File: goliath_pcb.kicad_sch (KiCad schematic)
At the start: 95 parts, among them IC1 MCT9001, IC2 MCT9001SD, IC3 MCT9001SD, IC4 MCT9001SD, IC5 MCT9001SD, IC6 MCT9001SD, IC7 MCT9001SD, J1 RJ45_LED, J10 Conn_01x04_Male, J11 Screw_Terminal_01x02, J12 Screw_Terminal_01x02, J13 Screw_Terminal_01x02, J14 Conn_01x02_Male, J15 Conn_01x02_Male, J2 RJ45_LED, J3 RJ45_LED, J4 RJ45_LED, J5 Conn_01x08_Male, J6 Conn_01x08_Male, J7 Conn_01x02_Male, J8 Conn_01x04_Male, J9 Conn_01x04_Male, Q1 STP2N80K5, Q2 STP2N80K5, U1 Pico, U2 LM2592HVT-5.0/NOPB, U3 74HCT244, U4 74HCT244, U5 MCP3008, U6 PCF8574, U7 PCF8574

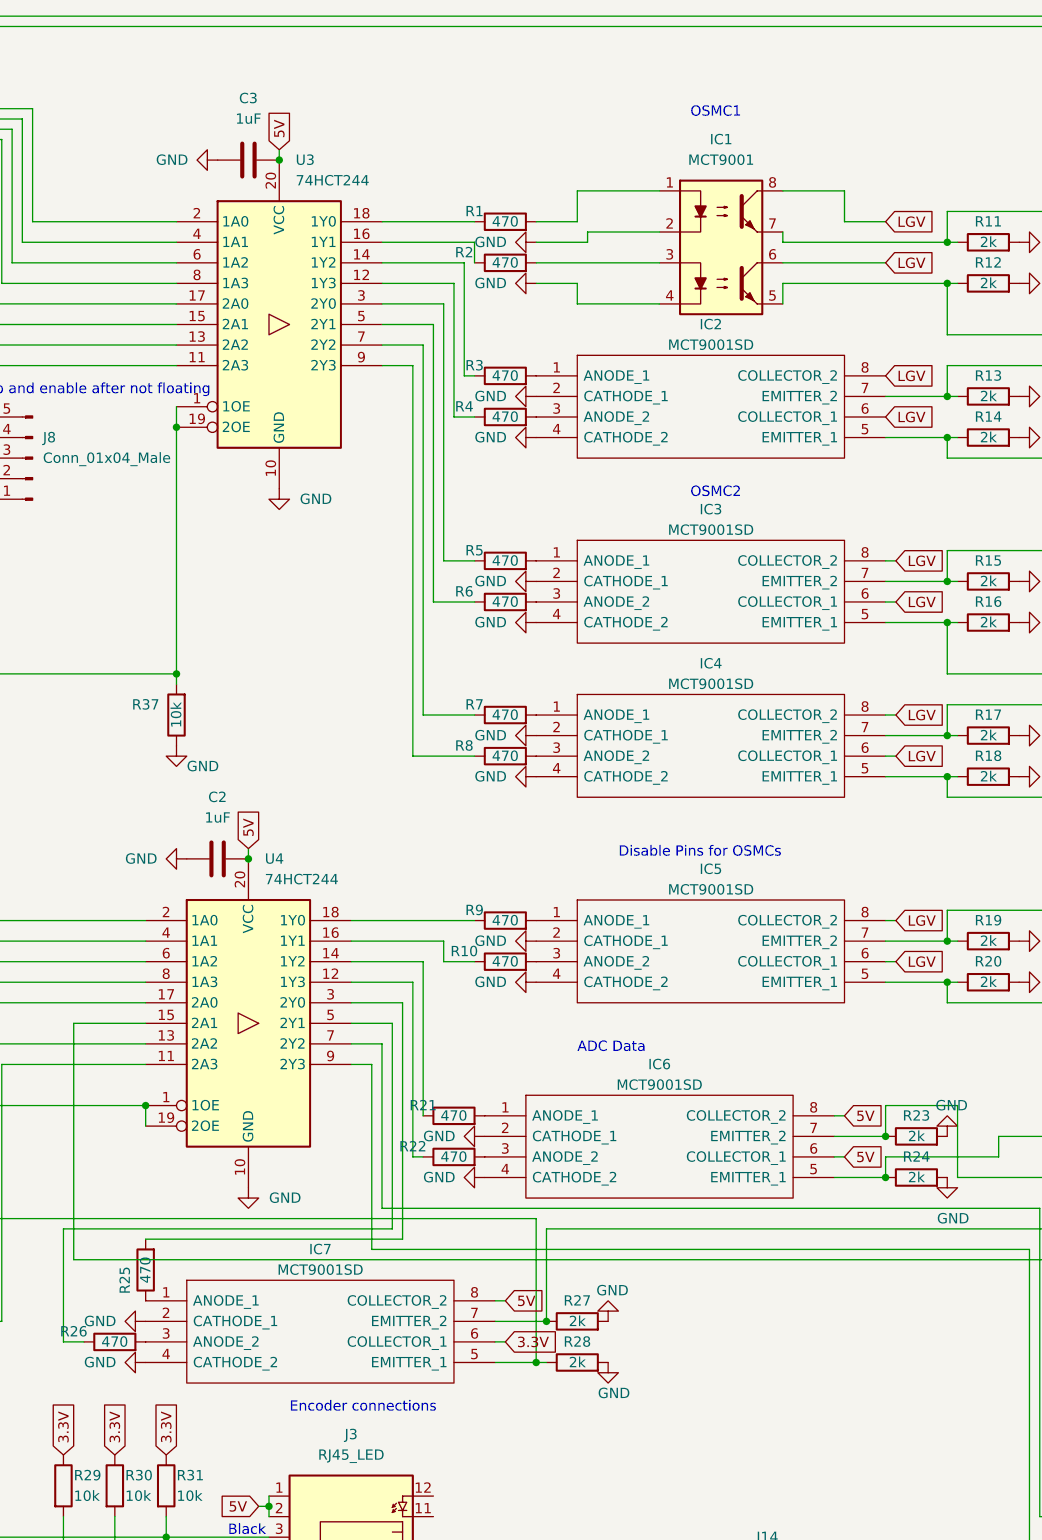
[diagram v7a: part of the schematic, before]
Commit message: Swap out all optocouplers (symbols, not the actual part)
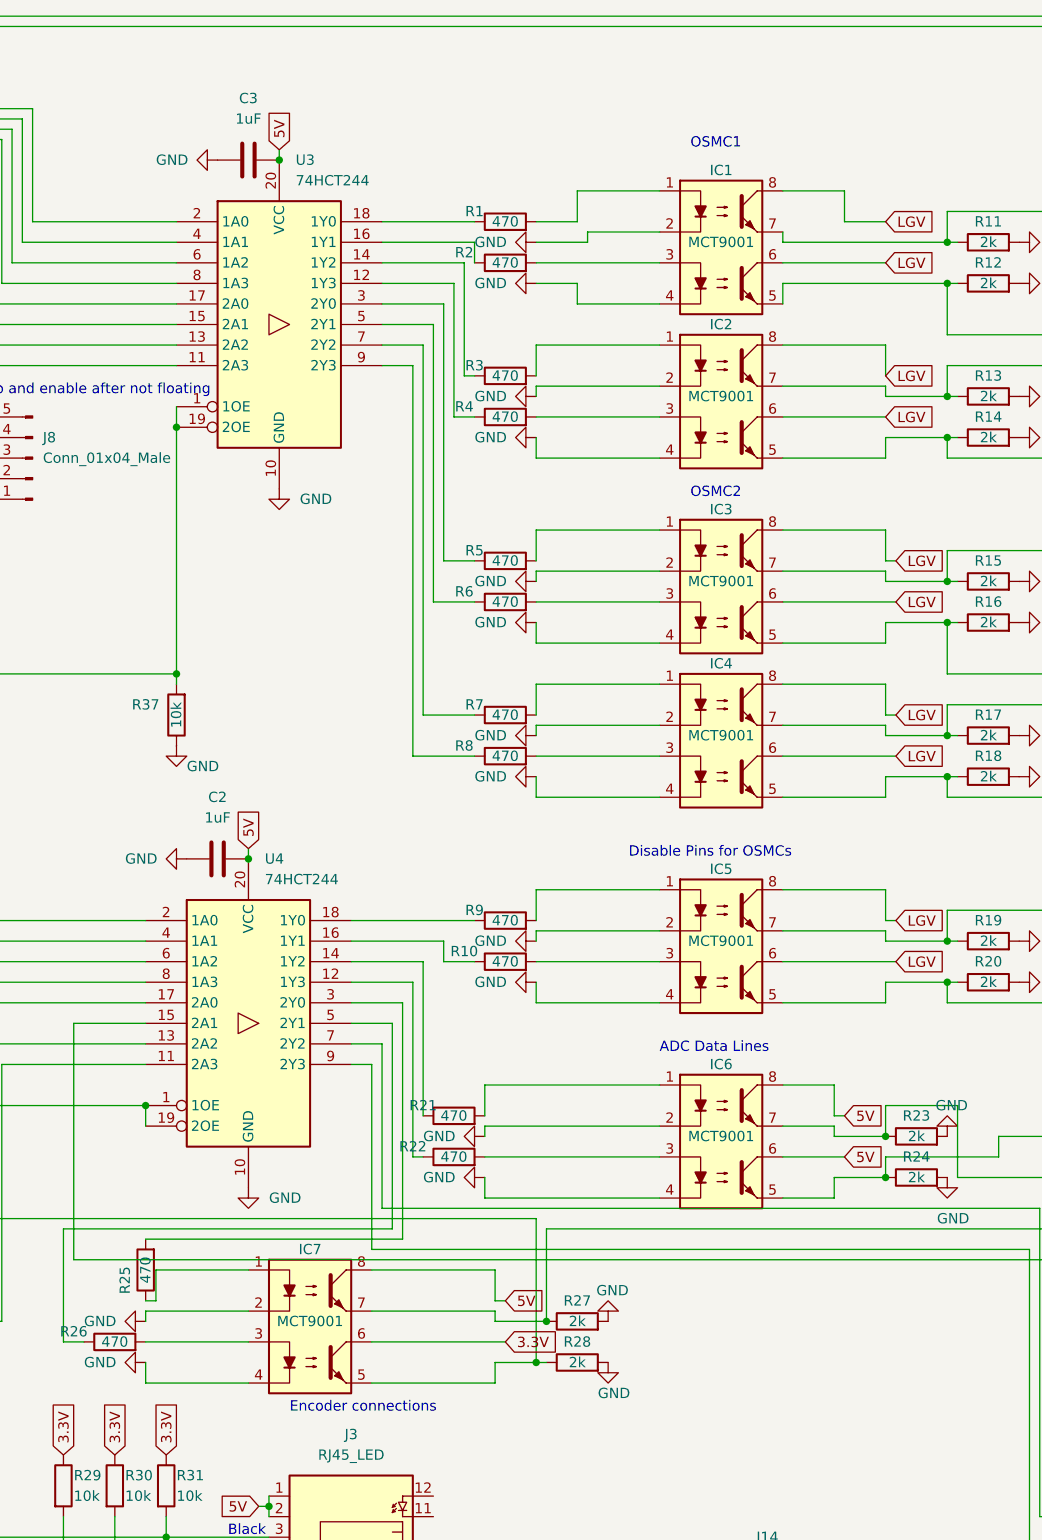
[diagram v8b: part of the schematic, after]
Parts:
- removed IC2, IC3, IC4, IC5, IC6, IC7: MCT9001SD, Package_DIP:DIP-8_W7.62mm_Socket, symbol MCT9001SD:MCT9001SD
- added IC2, IC3, IC4, IC5, IC6, IC7: MCT9001, Package_DIP:DIP-8_W7.62mm_Socket, symbol Optocoupler_AKL:MCT9001
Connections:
- net 3.3V: now also IC7.6
- net 5V: now also IC6.6, IC6.8, IC7.8
- net GND: now also IC2.2, IC2.4, IC3.2, IC3.4, IC4.2, IC4.4, IC5.2, IC5.4, IC6.2, IC6.4, IC7.2, IC7.4
- net LGV: now also IC2.6, IC2.8, IC3.6, IC3.8, IC4.6, IC4.8, IC5.6, IC5.8
- net at R24.1, U5.11 (Din): now also IC6.5
- net at R26.2: now also IC7.3
- net at R7.2: now also IC4.1
- net at R21.2: now also IC6.1
- net at R22.2: now also IC6.3
- net at R23.1, U5.13 (CLK): now also IC6.7
- net at J2.3, R20.1: now also IC5.5
- net at J1.3, R19.1: now also IC5.7
- net at J1.6, R13.1: now also IC2.7
- net at J1.7, R14.1: now also IC2.5
- net at J2.4, R16.1: now also IC3.5
- net at R10.2: now also IC5.3
- net at R5.2: now also IC3.1
- net at R6.2: now also IC3.3
- net at J2.5, R15.1: now also IC3.7
- net at R3.2: now also IC2.1
- net at R4.2: now also IC2.3
- net at R9.2: now also IC5.1
- net at J2.6, R17.1: now also IC4.7
- net at J2.7, R18.1: now also IC4.5
- net at R25.1: now also IC7.1
- net at R28.1, U1.16 (GPIO12): now also IC7.5
- net at R27.1, U5.10 (~{CS}/SHDN): now also IC7.7
- net at R8.2: now also IC4.3
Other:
- note added: "ADC Data Lines"
- note removed: "ADC Data"
